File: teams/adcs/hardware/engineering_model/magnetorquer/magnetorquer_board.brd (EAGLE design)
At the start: 90 x 90 mm, 38 parts

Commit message: ADCS/MT: PCB revision
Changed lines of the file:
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@@
 <?xml version="1.0" encoding="utf-8"?>
 <!DOCTYPE eagle SYSTEM "eagle.dtd">
-<eagle version="7.5.0">
+<eagle version="8.4.1">
 <drawing>
 <settings>
 <setting alwaysvectorfont="no"/>
+<setting keepoldvectorfont="yes"/>
 <setting verticaltext="up"/>
 </settings>
@@
 <param name="dpMaxLengthDifference" value="10mm"/>
 <param name="dpGapFactor" value="2.5"/>
-<param name="checkGrid" value="0"/>
 <param name="checkAngle" value="0"/>
 <param name="checkFont" value="1"/>
 <param name="checkRestrict" value="1"/>
+<param name="checkStop" value="0"/>
 <param name="useDiameter" value="13"/>
 <param name="maxErrors" value="50"/>
@@
 <contactref element="U$6" pad="P$6"/>
 <contactref element="C1" pad="1"/>
-<contactref element="R4" pad="1"/>
 <contactref element="L1" pad="P$4"/>
 <wire x1="84.705" y1="47.28" x2="84.705" y2="47.875" width="0.254" layer="1"/>
@@
 <wire x1="85.24875" y1="48.41875" x2="85.7275" y2="48.8975" width="0.508" layer="1"/>
 <wire x1="81.5975" y1="47.9425" x2="81.915" y2="47.9425" width="0.254" layer="1"/>
-<wire x1="81.5975" y1="47.9425" x2="81.595" y2="47.9425" width="0.254" layer="1"/>
 <wire x1="85.7275" y1="49.8475" x2="84.7725" y2="49.8475" width="0.254" layer="1"/>
 <wire x1="84.7725" y1="49.8475" x2="84.320915625" y2="49.395915625" width="0.254" layer="1"/>
@@
 <wire x1="62.484" y1="73.914" x2="62.992" y2="73.914" width="0.6096" layer="16"/>
 <contactref element="JP2" pad="1"/>
+<contactref element="R4" pad="1"/>
 <wire x1="90.424" y1="71.374" x2="89.662" y2="71.882" width="0" layer="19" extent="1-1"/>
+<wire x1="81.595" y1="47.9425" x2="81.5975" y2="47.9425" width="0" layer="19" extent="1-1"/>
+<wire x1="77.978" y1="80.648" x2="77.978" y2="75.568" width="0" layer="19" extent="1-1"/>
 </signal>
 <signal name="N$1">

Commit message: ADCS/MT: Update LDO and PC104 stack board
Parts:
- LDO_3V1, LDO_5V1: value LINEAR_LDO_LT1761-X -> TPS732XX
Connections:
- net GND: now also U$1.P$87; no longer U$1.P$86
- net VBAT: now also U$1.P$86; no longer U$1.P$87

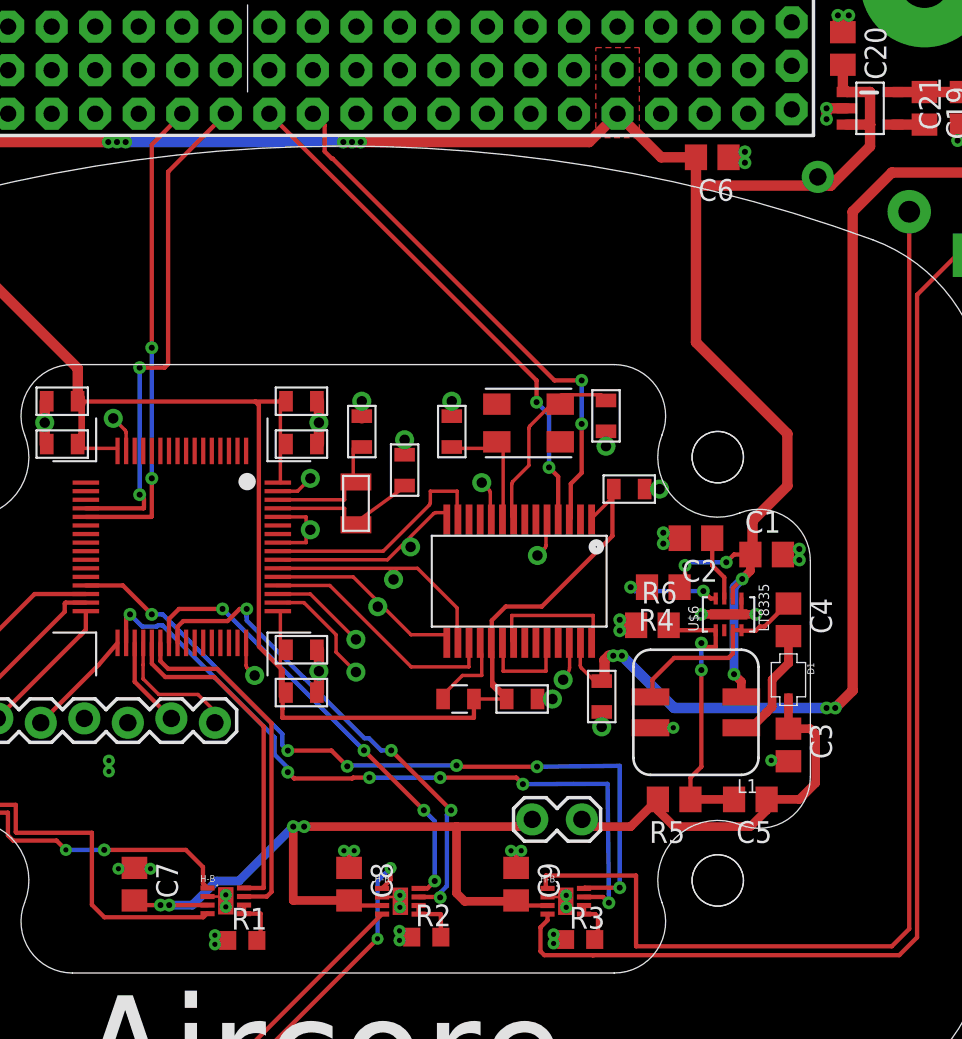
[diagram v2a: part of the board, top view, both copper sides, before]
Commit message: ADCS/MT: Reconnect to stack and use new SEPIC layout
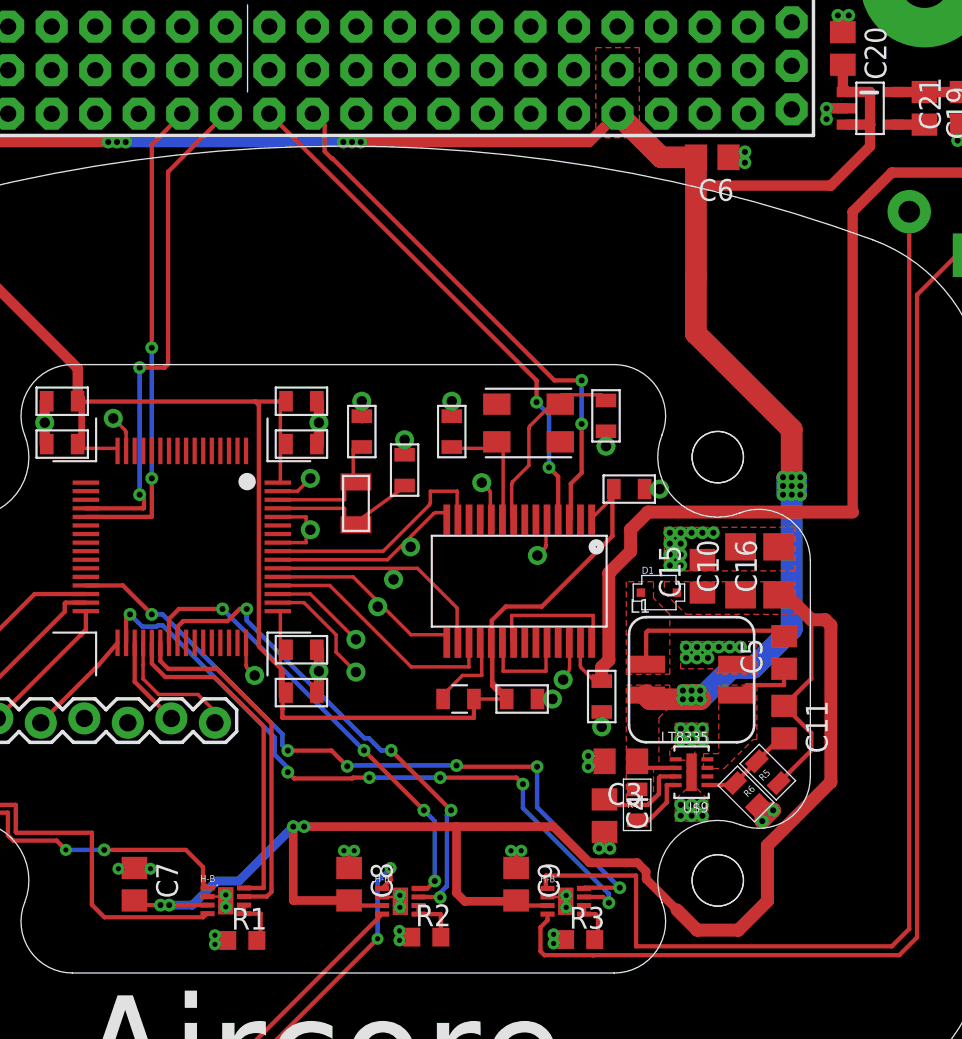
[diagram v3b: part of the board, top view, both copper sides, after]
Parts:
- removed C1, C2: (no value), rcl:C0805
- removed JP1: M02LOCK, SparkFun-Connectors:1X02_LOCK
- removed JP2: M01NOSILK-KIT, SparkFun-Connectors:1X01NS-KIT
- removed U$6: LT8335, DubSat1 Components:DDB
- added C10: 22 uF, rcl:C1206
- added C11: 5.6 pF, rcl:C0805
- added C15: 10 uF, rcl:C0805
- added C16: 47 uF, rcl:C1206
- added U$9: LT8335, DubSat1 Components:DDB
- C12, C19: value 0.01 μF -> 0.01 uF
- C13, C20: value 1 μF -> 1 uF
- C14, C21: value 4.7 μF -> 4.7 uF
- C3: value (none) -> 2.2 μF
- C4: value (none) -> 2.2 uF
- C5: value (none) -> 1 uF
- C6: value (none) -> 10 uF
- R4: value (none) -> 1 kΩ; device rcl:R0805 -> DubSat1 Components:0805
- R5: value (none) -> 330 kΩ; device rcl:R0805 -> DubSat1 Components:0805
- R6: value (none) -> 120 kΩ; device rcl:R0805 -> DubSat1 Components:0805
- moved C4 15.7 mm to (77.2, 34.6)
- moved R4 12.8 mm to (79.1, 35.2), turned to 270 degrees
- moved R6 11.3 mm to (85.5, 35.9), turned to 135 degrees
- moved C3 9.83 mm to (78.2, 37.8), turned to 180 degrees
- moved D1 9.11 mm to (80.4, 47.6), turned to 0 degrees
- moved C5 8.80 mm to (87.7, 44.1), turned to 90 degrees
- moved R5 5.69 mm to (86.7, 37.1), turned to 315 degrees
- moved L1 1.92 mm to (82.3, 42.5), turned to 270 degrees
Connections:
- removed net EN_UVLO: R4.2, U$6.P$8
- removed net N$6: C4.2, D1.P$1, L1.P$1
- new net EN_UVLO1: R4.2, U$9.P$8
- new net VD: C5.2, D1.P$1, L1.P$1
- net 6V: now also C10.1, C11.1, C15.1, C16.1; no longer C3.1, C5.1, JP1.1, JP1.2
- net FBX: now also C11.2, U$9.P$1; no longer C5.2, U$6.P$1
- net GND: now also C10.2, C15.2, C16.2, C4.2, U$9.GND, U$9.P$5; no longer C1.2, C2.2, U$6.GND, U$6.P$5
- net INT_VCC: now also C4.1, U$9.P$7; no longer C2.1, U$6.P$7
- net SW: now also C5.1, U$9.P$3, U$9.P$4; no longer C4.1, U$6.P$3, U$6.P$4
- net VBAT: now also C3.1, U$9.P$6; no longer C1.1, JP2.1, U$6.P$6
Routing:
- net 6V: track 71.3 -> 100.0 mm
- net FBX: track 16.7 -> 5.26 mm, vias 2 -> 0
- net VD: track 0.00 -> 10.1 mm
- net VBAT: track 128.5 -> 137.3 mm, vias 10 -> 21
- net SW: track 11.7 -> 3.94 mm
- net N$6: track 6.82 -> 0.00 mm
- net EN_UVLO: track 6.19 -> 0.00 mm, vias 2 -> 0
- net GND: track 44.3 -> 38.3 mm, vias 44 -> 70
- net +5V: track 65.4 -> 59.4 mm, vias 4 -> 0
- net EN_UVLO1: track 0.00 -> 3.70 mm
- net PWM_Z_1: track 43.1 -> 40.2 mm
- net PWM_Z_2: track 45.2 -> 42.4 mm
- net INT_VCC: track 3.81 -> 5.53 mm
- added copper zone on layer 1, net 6V
- added copper zone on layer 1, net GND
- added copper zone on layer 1, net SW
- added copper zone on layer 1, net VD

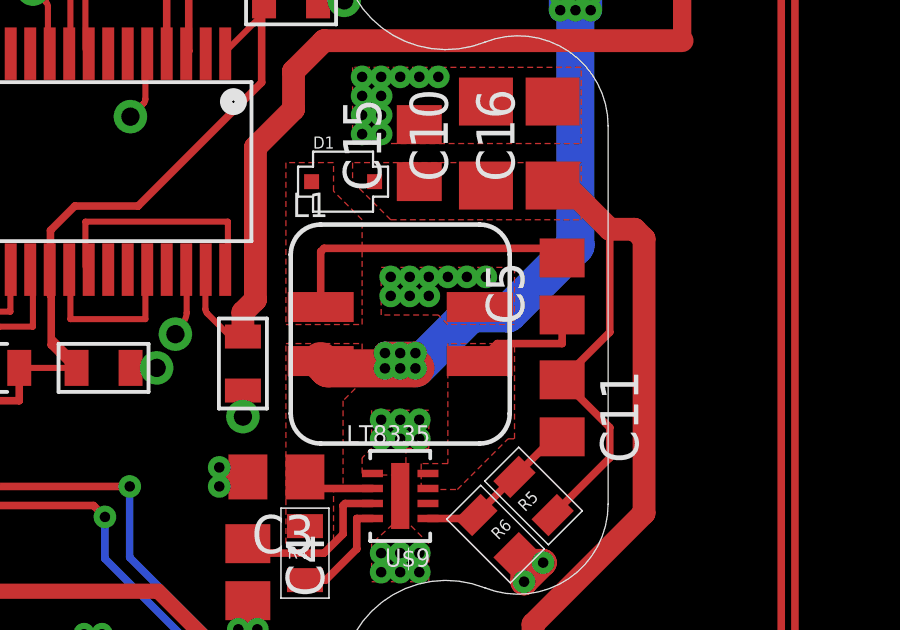
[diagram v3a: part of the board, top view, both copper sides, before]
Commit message: ADCS: Switch to new SEPIC layout
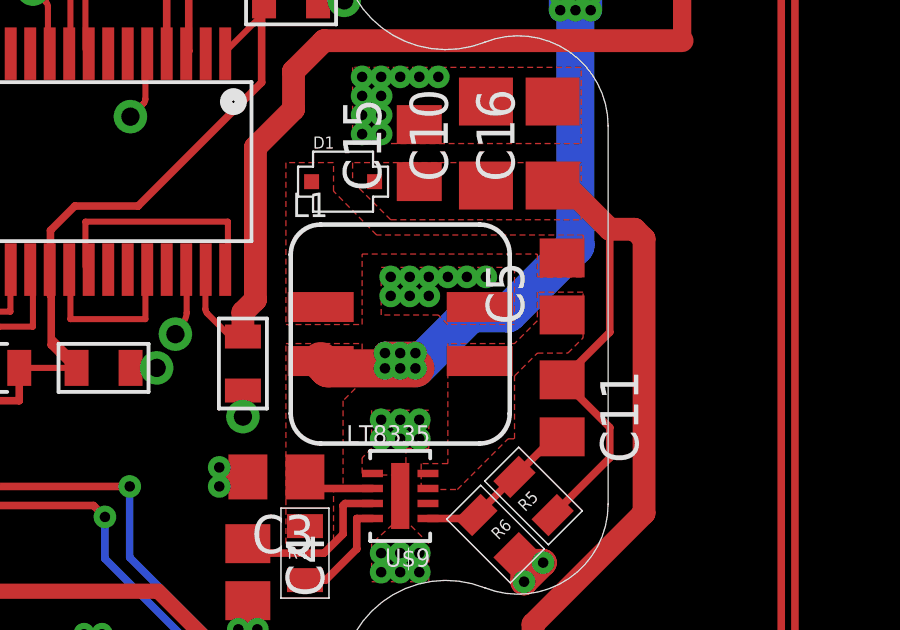
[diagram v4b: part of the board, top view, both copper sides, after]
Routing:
- net VD: track 10.1 -> 0.00 mm
- net SW: track 3.94 -> 0.00 mm
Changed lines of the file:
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@@
 <vertex x="85.8901" y="39.0525"/>
 <vertex x="86.106" y="39.0525"/>
+<vertex x="86.106" y="41.148"/>
+<vertex x="86.868" y="41.91"/>
+<vertex x="87.884" y="41.91"/>
+<vertex x="88.392" y="42.418"/>
+<vertex x="88.392" y="43.942"/>
+<vertex x="86.868" y="43.942"/>
+<vertex x="86.868" y="42.9895"/>
 <vertex x="86.106" y="42.2275"/>
 <vertex x="83.8835" y="42.2275"/>
@@
 <vertex x="82.9945" y="38.227"/>
 </polygon>
-<wire x1="87.6935" y1="43.1825" x2="87.6935" y2="42.2275" width="0.254" layer="1"/>
-<wire x1="87.6935" y1="42.2275" x2="85.5285" y2="42.2275" width="0.254" layer="1"/>
-<wire x1="85.5285" y1="42.2275" x2="84.946" y2="41.645" width="0.254" layer="1"/>
 </signal>
 <signal name="VD">
@@
 <vertex x="78.486" y="42.8625"/>
 <vertex x="81.026" y="42.8625"/>
-<vertex x="81.026" y="46.355"/>
+<vertex x="81.026" y="45.212"/>
+<vertex x="86.868" y="45.212"/>
+<vertex x="86.868" y="44.45"/>
+<vertex x="88.392" y="44.45"/>
+<vertex x="88.392" y="45.847"/>
+<vertex x="81.5086" y="45.847"/>
 <vertex x="80.0735" y="47.3075"/>
 <vertex x="80.0735" y="48.26"/>
 <vertex x="78.486" y="48.26"/>
 </polygon>
-<wire x1="87.6935" y1="45.0825" x2="87.3735" y2="45.4025" width="0.254" layer="1"/>
-<wire x1="87.3735" y1="45.4025" x2="79.756" y2="45.4025" width="0.254" layer="1"/>
-<wire x1="79.756" y1="45.4025" x2="79.646" y2="45.2925" width="0.254" layer="1"/>
-<wire x1="79.646" y1="45.2925" x2="79.646" y2="43.445" width="0.254" layer="1"/>
 </signal>
 <signal name="FBX">
